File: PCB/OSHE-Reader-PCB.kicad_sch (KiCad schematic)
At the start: 6 parts

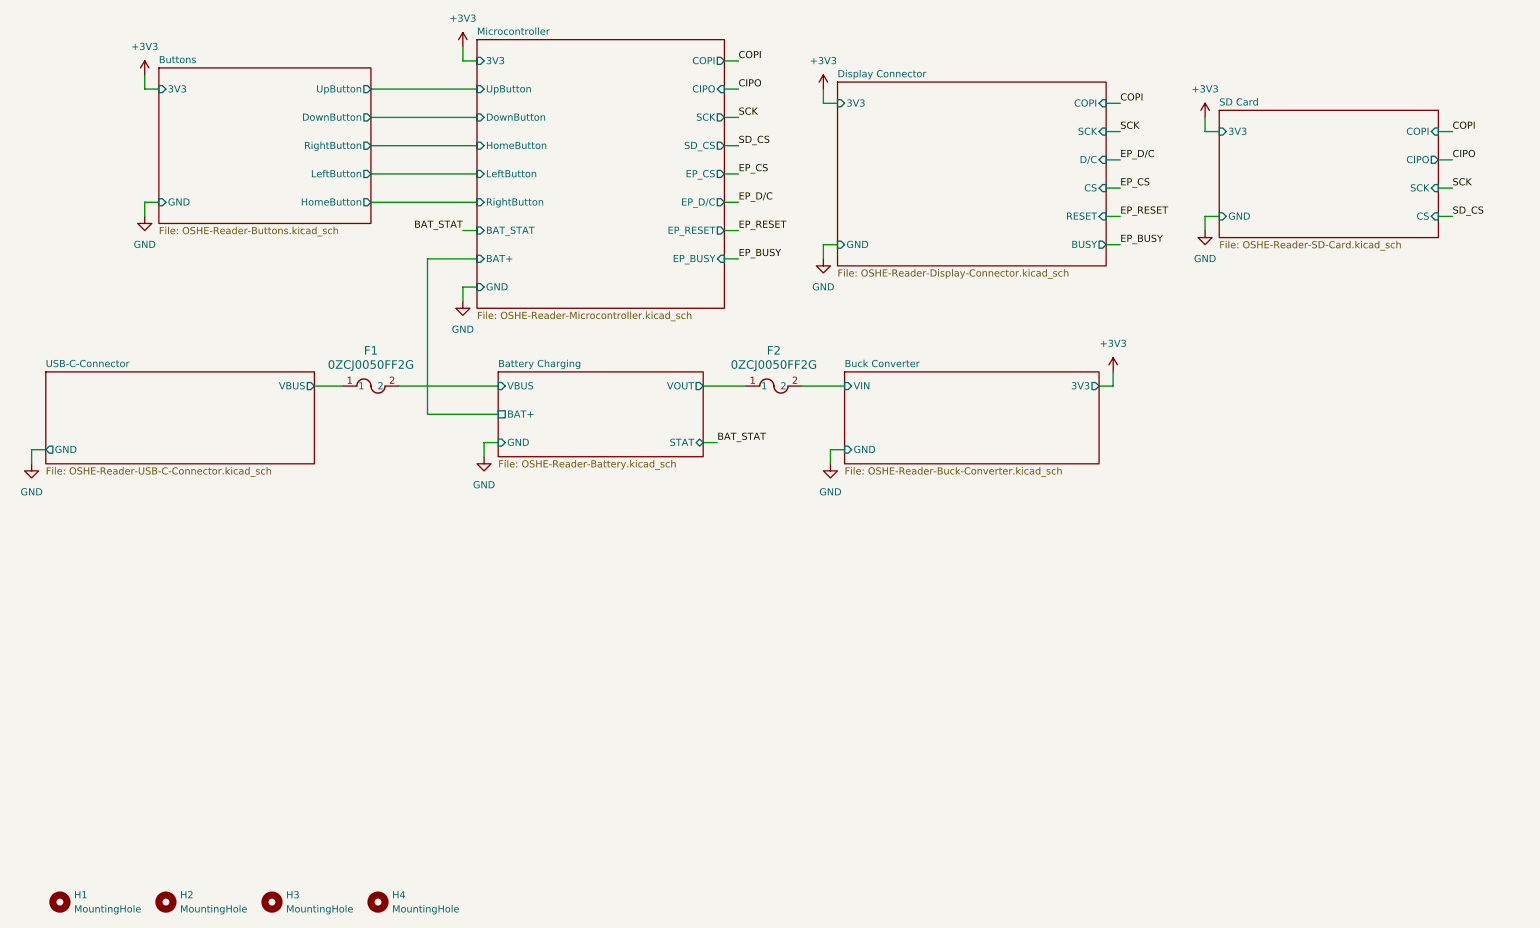
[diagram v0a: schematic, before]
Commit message: Added OSHE logo to backside of PCB, added info in bottom right of schematic
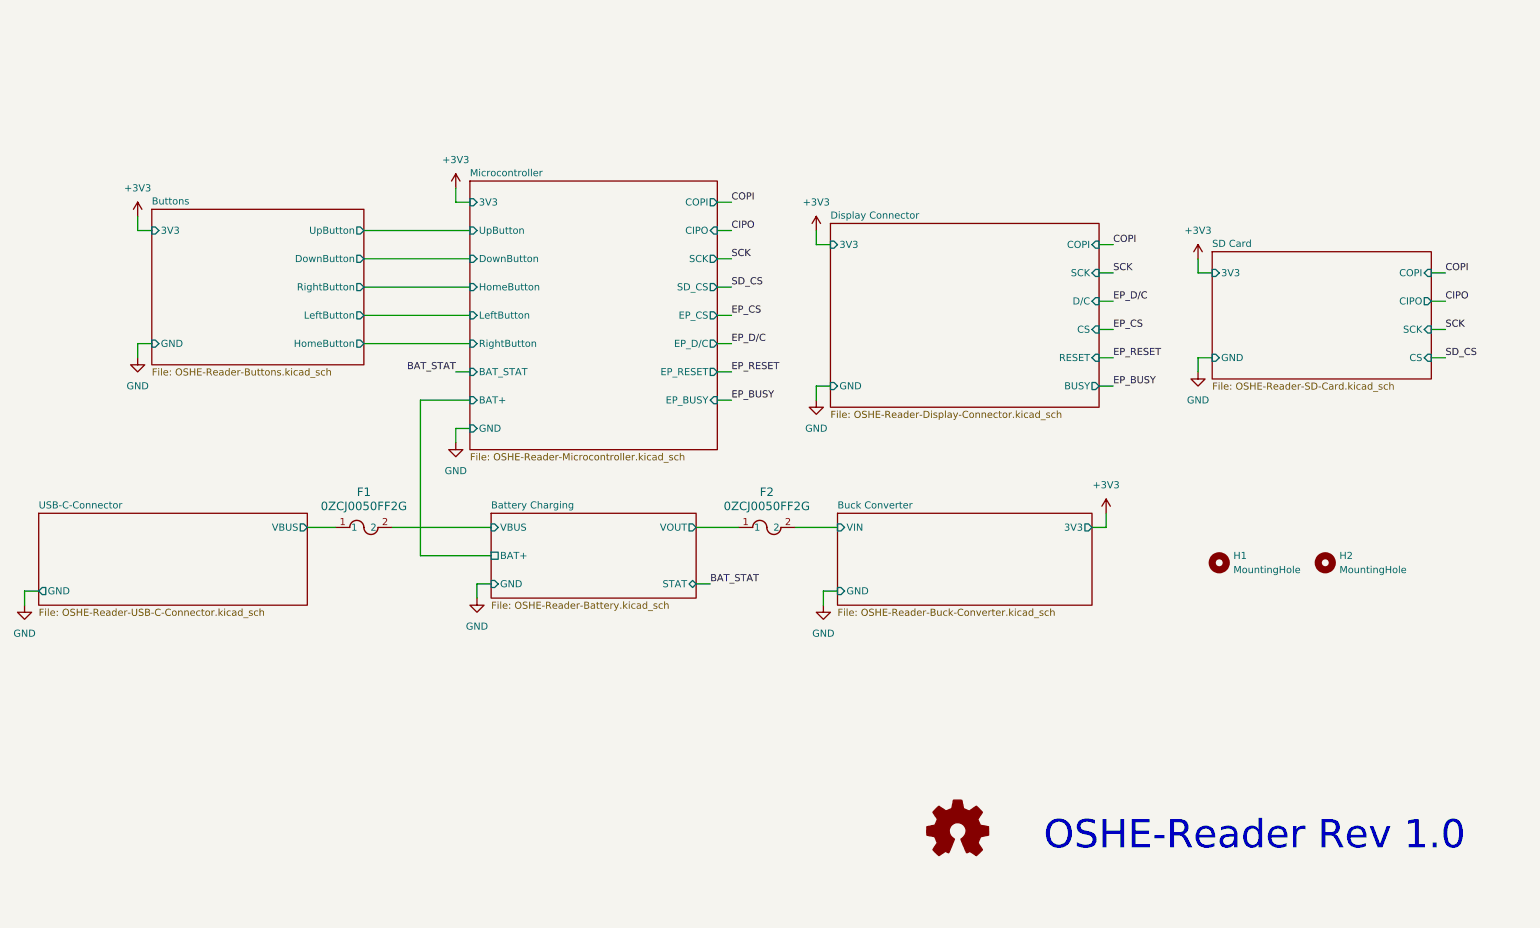
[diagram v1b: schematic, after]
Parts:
- removed H3, H4: MountingHole, MountingHole:MountingHole_3.2mm_M3, symbol Mechanical:MountingHole
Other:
- note added: "OSHE-Reader Rev 1.0"
- moved on the sheet: F1, F2, H1, H2

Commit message: Added a bunch of test points to schematic and pcb, hopefully not needed, but good to have :)
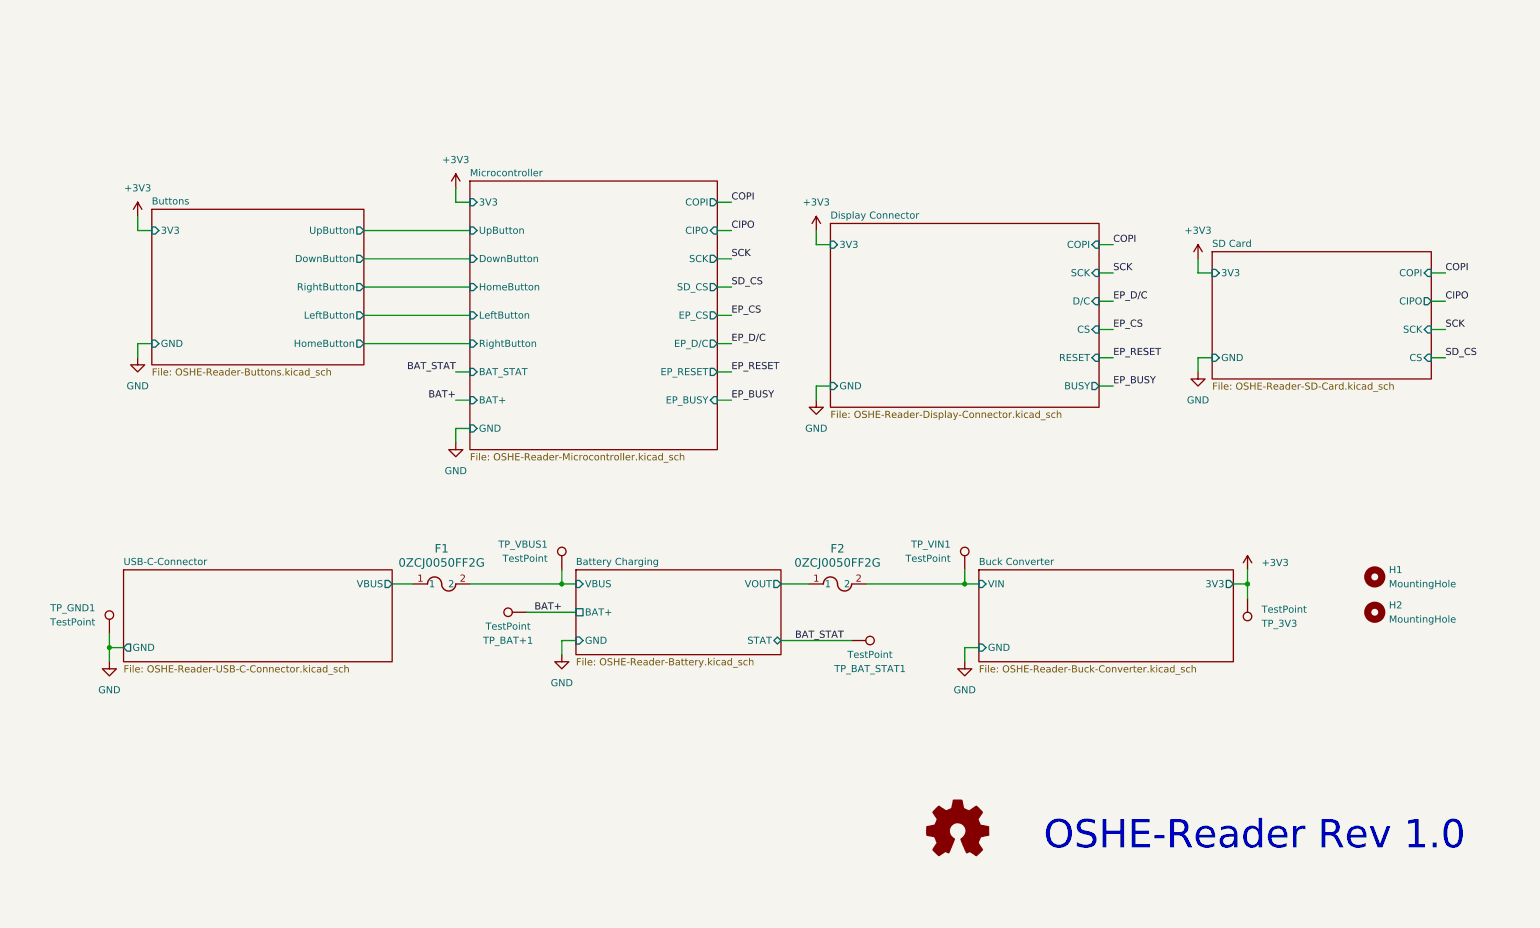
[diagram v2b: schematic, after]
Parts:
- added TP_3V3, TP_BAT+1, TP_BAT_STAT1, TP_GND1, TP_VBUS1, TP_VIN1: TestPoint, TestPoint:TestPoint_Keystone_5019_Miniature, symbol Connector:TestPoint
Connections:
- net +3V3: now also TP_3V3.1
- net BAT_STAT: now also TP_BAT_STAT1.1
- net Battery Charging/VBUS: now also TP_VBUS1.1
- net Buck Converter/VIN: now also TP_VIN1.1
- net GND: now also TP_GND1.1
- new net BAT+: TP_BAT+1.1
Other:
- moved on the sheet: F1, F2, H1, H2

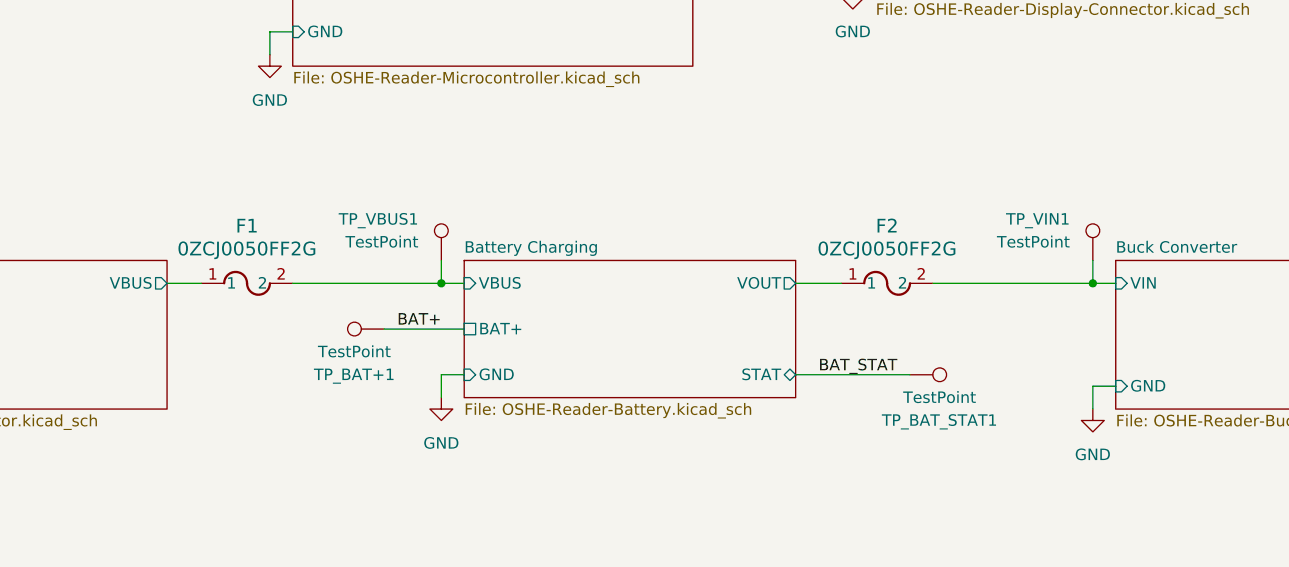
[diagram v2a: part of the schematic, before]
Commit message: Did a bunch of work: - Updated footprint libs with proper 3d models to fix models dissapearing on update from pcb - Updated footprint libs with better silkscreen for drc - Re-did ESP32-C6 Footprint to support through hole AND castellated edges (espressif & waveshare) - Rerouted PCB around new MCU footprint - Minor cleanup on schematic + extra GND test point for convienience using O-Scope
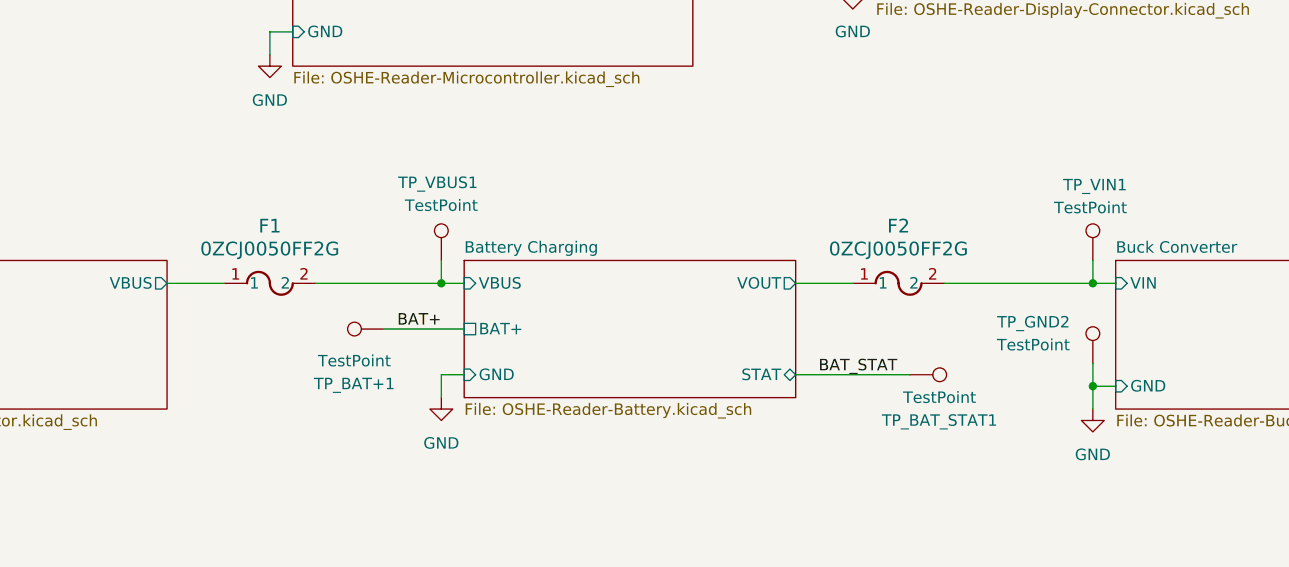
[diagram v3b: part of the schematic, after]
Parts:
- added TP_GND2: TestPoint, TestPoint:TestPoint_Keystone_5019_Miniature, symbol Connector:TestPoint
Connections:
- net GND: now also TP_GND2.1
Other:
- moved on the sheet: F1, F2
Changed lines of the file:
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@@
+	)
+	(junction
+		(at 186.69 140.97)
+		(diameter 0)
+		(color 0 0 0 0)
 	)
 	(junction
@@
 	(wire
 		(pts
-			(xy 153.67 129.54) (xy 158.75 129.54)
+			(xy 153.67 129.54) (xy 160.02 129.54)
 		)
 		(stroke
@@
 	(wire
 		(pts
-			(xy 97.79 129.54) (xy 114.3 129.54)
+			(xy 100.33 129.54) (xy 114.3 129.54)
 		)
 		(stroke
@@
 	(wire
 		(pts
+			(xy 186.69 138.43) (xy 186.69 140.97)
+		)
+		(stroke
+			(width 0)
+			(type default)
+		)
+	)
+	(wire
+		(pts
 			(xy 186.69 127) (xy 186.69 129.54)
 		)
@@
 	(wire
 		(pts
-			(xy 83.82 129.54) (xy 87.63 129.54)
+			(xy 83.82 129.54) (xy 90.17 129.54)
 		)
 		(stroke
@@
 	(wire
 		(pts
-			(xy 168.91 129.54) (xy 186.69 129.54)
+			(xy 170.18 129.54) (xy 186.69 129.54)
 		)
 		(stroke
@@
 	(symbol
 		(lib_id "0ZCJ0050FF2G:0ZCJ0050FF2G")
-		(at 87.63 129.54 0)
+		(at 90.17 129.54 0)
 		(unit 1)
 		(exclude_from_sim no)
@@
 		(fields_autoplaced yes)
 		(property "Reference" "F1"
-			(at 92.71 123.19 0)
+			(at 95.25 123.19 0)
 			(effects
 				(font
@@
 		)
 		(property "Value" "0ZCJ0050FF2G"
-			(at 92.71 125.73 0)
+			(at 95.25 125.73 0)
 			(effects
 				(font
@@
 		)
 		(property "Footprint" "0ZCJ0050FF2G:0ZCJ_BEL"
-			(at 87.63 129.54 0)
+			(at 90.17 129.54 0)
 			(effects
 				(font
@@
 		)
 		(property "Datasheet" "0ZCJ0050FF2G"
-			(at 87.63 129.54 0)
+			(at 90.17 129.54 0)
 			(effects
 				(font
@@
 		)
 		(property "Description" ""
-			(at 87.63 129.54 0)
+			(at 90.17 129.54 0)
 			(effects
 				(font
@@
 		(dnp no)
 		(property "Reference" "TP_BAT+1"
-			(at 104.648 139.7 90)
+			(at 104.648 140.716 90)
 			(effects
 				(font
@@
 		)
 		(property "Value" "TestPoint"
-			(at 104.648 137.16 90)
+			(at 104.648 138.176 90)
 			(effects
 				(font
@@
 	(symbol
 		(lib_id "0ZCJ0050FF2G:0ZCJ0050FF2G")
-		(at 158.75 129.54 0)
+		(at 160.02 129.54 0)
 		(unit 1)
 		(exclude_from_sim no)
@@
 		(fields_autoplaced yes)
 		(property "Reference" "F2"
-			(at 163.83 123.19 0)
+			(at 165.1 123.19 0)
 			(effects
 				(font
@@
 		)
 		(property "Value" "0ZCJ0050FF2G"
-			(at 163.83 125.73 0)
+			(at 165.1 125.73 0)
 			(effects
 				(font
@@
 		)
 		(property "Footprint" "0ZCJ0050FF2G:0ZCJ_BEL"
-			(at 158.75 129.54 0)
+			(at 160.02 129.54 0)
 			(effects
 				(font
@@
 		)
 		(property "Datasheet" "0ZCJ0050FF2G"
-			(at 158.75 129.54 0)
+			(at 160.02 129.54 0)
 			(effects
 				(font
@@
 		)
 		(property "Description" ""
-			(at 158.75 129.54 0)
+			(at 160.02 129.54 0)
 			(effects
 				(font
@@
 				(path "/3f072c92-e35a-4654-839b-728bd3dc3a46"
 					(reference "F2")
+					(unit 1)
+				)
+			)
+		)
+	)
+	(symbol
+		(lib_id "Connector:TestPoint")
+		(at 186.69 138.43 0)
+		(mirror y)
+		(unit 1)
+		(exclude_from_sim no)
+		(in_bom yes)
+		(on_board yes)
+		(dnp no)
+		(property "Reference" "TP_GND2"
+			(at 184.15 133.8579 0)
+			(effects
+				(font
+					(size 1.27 1.27)
+				)
+				(justify left)
+			)
+		)
+		(property "Value" "TestPoint"
+			(at 184.15 136.3979 0)
+			(effects
+				(font
+					(size 1.27 1.27)
+				)
+				(justify left)
+			)
+		)
+		(property "Footprint" "TestPoint:TestPoint_Keystone_5019_Miniature"
+			(at 181.61 138.43 0)
+			(effects
+				(font
+					(size 1.27 1.27)
+				)
+				(hide yes)
+			)
+		)
+		(property "Datasheet" "~"
+			(at 181.61 138.43 0)
+			(effects
+				(font
+					(size 1.27 1.27)
+				)
+				(hide yes)
+			)
+		)
+		(property "Description" "test point"
+			(at 186.69 138.43 0)
+			(effects
+				(font
+					(size 1.27 1.27)
+				)
+				(hide yes)
+			)
+		)
+		(pin "1"
+		)
+		(instances
+			(project "OSHE-Reader-PCB"
+				(path "/3f072c92-e35a-4654-839b-728bd3dc3a46"
+					(reference "TP_GND2")
 					(unit 1)
 				)
@@
 		(dnp no)
 		(property "Reference" "TP_VBUS1"
-			(at 111.76 122.4279 0)
+			(at 118.364 118.3639 0)
 			(effects
 				(font
@@
 		)
 		(property "Value" "TestPoint"
-			(at 111.76 124.9679 0)
+			(at 118.364 120.9039 0)
 			(effects
 				(font
@@
 		(dnp no)
 		(property "Reference" "TP_VIN1"
-			(at 184.15 122.4279 0)
+			(at 190.5 118.6179 0)
 			(effects
 				(font
@@
 		)
 		(property "Value" "TestPoint"
-			(at 184.15 124.9679 0)
-			(effects
-				(font
+			(at 190.5 121.1579 0)
+			(effects
+				(font

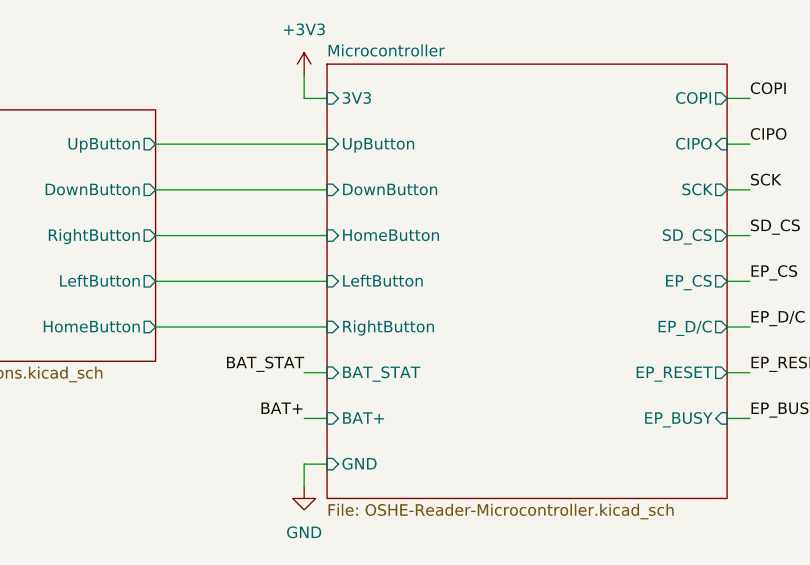
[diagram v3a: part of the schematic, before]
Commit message: Last updates for PCB order. Added revision number, fanicied logo, finished button positions, TODO: Blizzard T. Husky signature :P
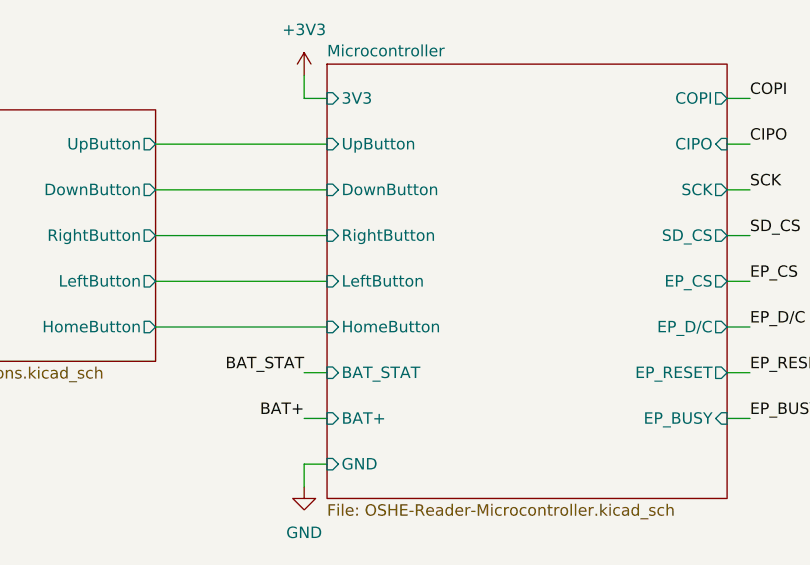
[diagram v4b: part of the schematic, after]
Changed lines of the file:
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@@
 			)
 		)
-		(pin "HomeButton" input
+		(pin "RightButton" input
 			(at 97.79 76.2 180)
 			(effects
@@
 			)
 		)
-		(pin "RightButton" input
+		(pin "HomeButton" input
 			(at 97.79 86.36 180)
 			(effects
